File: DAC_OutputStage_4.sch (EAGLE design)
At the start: 56 parts, among them J1 1935190, J3 SJ-63033A

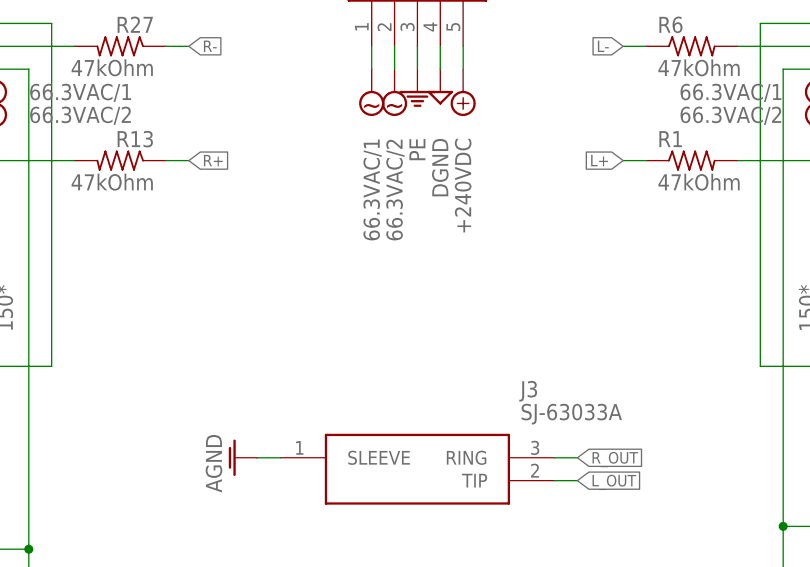
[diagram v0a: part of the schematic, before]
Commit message: Update Output stage with fusion export
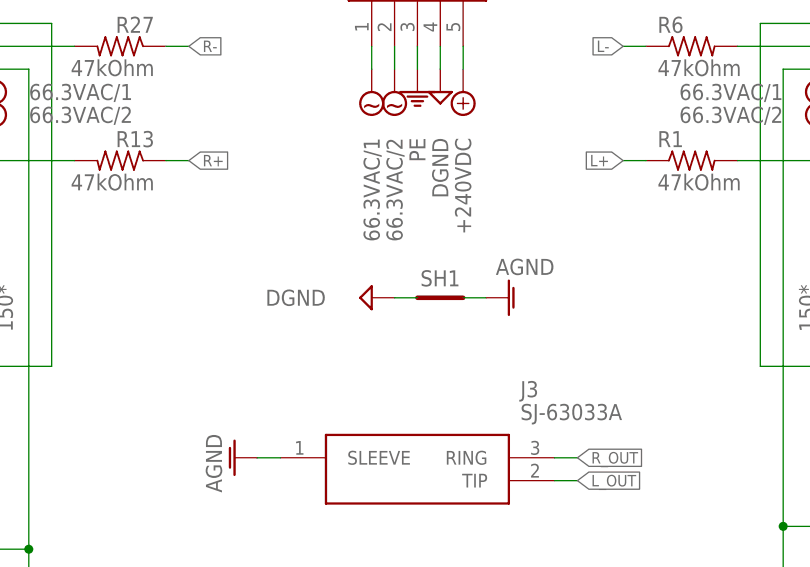
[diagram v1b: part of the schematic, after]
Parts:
- added SH1: SHORTA5, Dual Mono Amp Library:SHORTA5
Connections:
- net AGND: now also SH1.P$2
- net DGND: now also SH1.P$1

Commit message: Combi progress
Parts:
- renumbered C1 to C1O, C10 to C10O, C11 to C11O, C12 to C12O, C13 to C13O, C14 to C14O, C15 to C15O, C16 to C16O, C18 to C18O, C2 to C2O, C21 to C21O, C23 to C23O, C24 to C24O, C25 to C25O, C26 to C26O, C4 to C4O, C5 to C5O, C6 to C6O, C7 to C7O, C9 to C9O, R1 to R1O, R10 to R10O, R11 to R11O, R12 to R12O, R13 to R13O, R14 to R14O, R15 to R15O, R16 to R16O, R17 to R17O, R18 to R18O, R19 to R19O, R2 to R2O, R20 to R20O, R21 to R21O, R22 to R22O, R23 to R23O, R24 to R24O, R25 to R25O, R26 to R26O, R27 to R27O, R28 to R28O, R29 to R29O, R3 to R3O, R30 to R30O, R4 to R4O, R5 to R5O, R6 to R6O, R7 to R7O, R8 to R8O, R9 to R9O
